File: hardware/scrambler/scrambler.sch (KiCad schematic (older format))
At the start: 20 parts, among them J1 Input, J2 Output, J3 Display

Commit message: Rev 1.1 of scrambler Software for scrambler
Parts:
- added R7: 330, Resistor_THT:R_Axial_DIN0207_L6.3mm_D2.5mm_P10.16mm_Horizontal, symbol Device:R_US
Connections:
- wire segments 82 -> 87
- no-connect marks 12 -> 10
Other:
- moved on the sheet: D1, D2, D3, D4, D5, D6, J1, R1, R2, R3, R4, R5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

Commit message: Fixup libraries. Rebrand.
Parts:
- A1: symbol MCU_Module:Arduino_UNO_R3 -> DMXDemonstrator:Arduino_UNO_R3-MCU_Module
- S1, S2, S3: symbol SparkFun-Switches:MOMENTARY-SWITCH-SPST-PTH-12MM -> DMXDemonstrator:MOMENTARY-SWITCH-SPST-PTH-12MM-SparkFun-Switches
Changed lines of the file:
@@
 EESchema Schematic File Version 4
-LIBS:scrambler-cache
-EELAYER 26 0
+EELAYER 30 0
 EELAYER END
 $Descr A4 11693 8268
@@
 Date "2023-12-24"
 Rev "1.1"
-Comp "Crazy Giraffe Software"
+Comp "Sparky Bobo Designs"
 Comment1 ""
 Comment2 "Designed by: SparkyBobo"
@@
 $EndDescr
 $Comp
-L MCU_Module:Arduino_UNO_R3 A1
+L DMXDemonstrator:Arduino_UNO_R3-MCU_Module A1
 U 1 1 5F3035A0
 P 6200 3350
@@
 Connection ~ 4250 3850
 $Comp
-L SparkFun-Switches:MOMENTARY-SWITCH-SPST-PTH-12MM S1
+L DMXDemonstrator:MOMENTARY-SWITCH-SPST-PTH-12MM-SparkFun-Switches S1
 U 1 1 5F53A7F8
 P 4550 3200
@@
 $EndComp
 $Comp
-L SparkFun-Switches:MOMENTARY-SWITCH-SPST-PTH-12MM S2
+L DMXDemonstrator:MOMENTARY-SWITCH-SPST-PTH-12MM-SparkFun-Switches S2
 U 1 1 5F53A858
 P 4550 3550
@@
 $EndComp
 $Comp
-L SparkFun-Switches:MOMENTARY-SWITCH-SPST-PTH-12MM S3
+L DMXDemonstrator:MOMENTARY-SWITCH-SPST-PTH-12MM-SparkFun-Switches S3
 U 1 1 5F53A8A0
 P 4550 3850

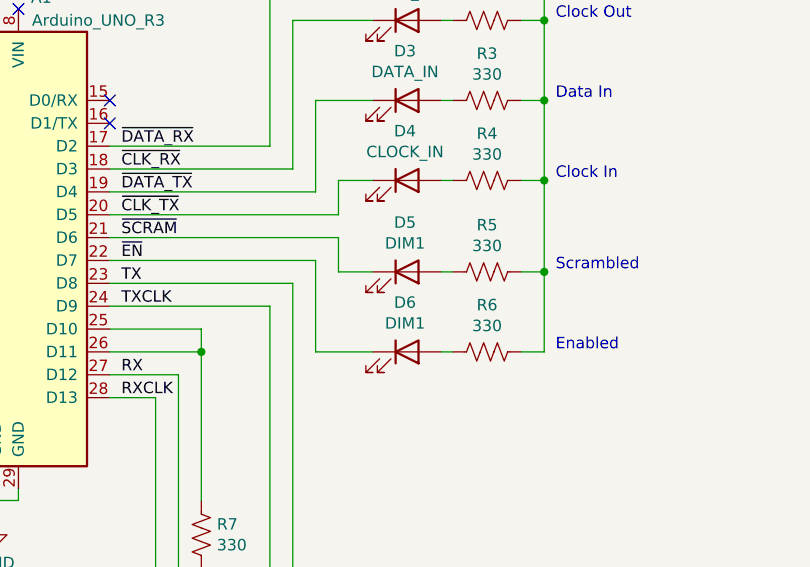
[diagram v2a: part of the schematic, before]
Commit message: Users/sparky/hwcleanup (#22)
* Rename control-pro
Update readmes
Delete old pngs

* Add PWM headers on DMX-RX1.

* Add BOM generator
Add BOM and parts .md's
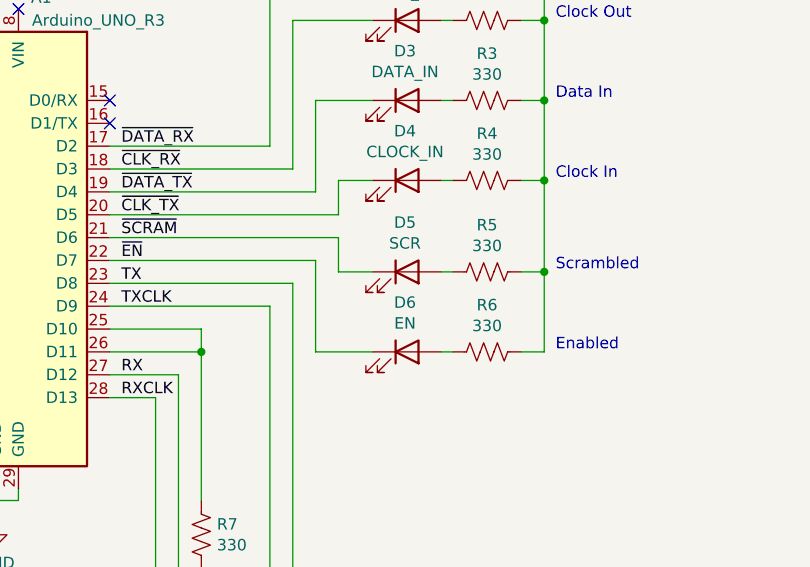
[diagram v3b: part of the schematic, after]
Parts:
- A1: PArtId2 (none) -> H_ARDUINO; PartId0 (none) -> PCB_FS1; PartId1 (none) -> A_ARDUINO
- D1, D3: PartId (none) -> LED_GRN
- D2, D4: PartId (none) -> LED_RED
- D5: value DIM1 -> SCR; PartId (none) -> LED_RED
- D6: value DIM1 -> EN; PartId (none) -> LED_GRN
- J1: PartId (none) -> H_1x3_RA,JP_1x3
- J2, J3: PartId (none) -> H_1x3_RA
- R1, R2, R3, R4, R5, R6, R7: PartId (none) -> R_LED
- S1, S2, S3: Field4 SWCH-09185 -> (none); PartId (none) -> S_MOM
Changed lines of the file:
@@
 F 2 "footprints:ARDUINO_R3_NO_HOLES" H 6350 2300 50  0001 L CNN
 F 3 "https://www.arduino.cc/en/Main/arduinoBoardUno" H 6000 4400 50  0001 C CNN
+F 4 "PCB_FS1" H 6200 3350 50  0001 C CNN "PartId0"
+F 5 "A_ARDUINO" H 6200 3350 50  0001 C CNN "PartId1"
+F 6 "H_ARDUINO" H 6200 3350 50  0001 C CNN "PArtId2"
 	1    6200 3350
 	-1   0    0    -1
@@
 F 2 "Connector_PinHeader_2.54mm:PinHeader_1x03_P2.54mm_Horizontal" H 4300 5000 50  0001 C CNN
 F 3 "~" H 4300 5000 50  0001 C CNN
+F 4 "H_1x3_RA" H 4300 5000 50  0001 C CNN "PartId"
 	1    4300 5000
 	-1   0    0    -1
@@
 F 2 "LED_THT:LED_D5.0mm" H 8000 2050 50  0001 C CNN
 F 3 "~" H 8000 2050 50  0001 C CNN
+F 4 "LED_GRN" H 8000 2050 50  0001 C CNN "PartId"
 	1    8000 2050
 	1    0    0    -1
@@
 F 2 "Resistor_THT:R_Axial_DIN0207_L6.3mm_D2.5mm_P10.16mm_Horizontal" V 8390 2040 50  0001 C CNN
 F 3 "~" H 8350 2050 50  0001 C CNN
+F 4 "R_LED" V 8350 2050 50  0001 C CNN "PartId"
 	1    8350 2050
 	0    1    1    0
@@
 F 2 "LED_THT:LED_D5.0mm" H 8000 2400 50  0001 C CNN
 F 3 "~" H 8000 2400 50  0001 C CNN
+F 4 "LED_RED" H 8000 2400 50  0001 C CNN "PartId"
 	1    8000 2400
 	1    0    0    -1
@@
 F 2 "Resistor_THT:R_Axial_DIN0207_L6.3mm_D2.5mm_P10.16mm_Horizontal" V 8390 2390 50  0001 C CNN
 F 3 "~" H 8350 2400 50  0001 C CNN
+F 4 "R_LED" V 8350 2400 50  0001 C CNN "PartId"
 	1    8350 2400
 	0    1    1    0
@@
 F 2 "LED_THT:LED_D5.0mm" H 8000 3100 50  0001 C CNN
 F 3 "~" H 8000 3100 50  0001 C CNN
+F 4 "LED_RED" H 8000 3100 50  0001 C CNN "PartId"
 	1    8000 3100
 	1    0    0    -1
@@
 F 2 "Resistor_THT:R_Axial_DIN0207_L6.3mm_D2.5mm_P10.16mm_Horizontal" V 8390 3090 50  0001 C CNN
 F 3 "~" H 8350 3100 50  0001 C CNN
+F 4 "R_LED" V 8350 3100 50  0001 C CNN "PartId"
 	1    8350 3100
 	0    1    1    0
@@
 F 2 "LED_THT:LED_D5.0mm" H 8000 2750 50  0001 C CNN
 F 3 "~" H 8000 2750 50  0001 C CNN
+F 4 "LED_GRN" H 8000 2750 50  0001 C CNN "PartId"
 	1    8000 2750
 	1    0    0    -1
@@
 F 2 "Resistor_THT:R_Axial_DIN0207_L6.3mm_D2.5mm_P10.16mm_Horizontal" V 8390 2740 50  0001 C CNN
 F 3 "~" H 8350 2750 50  0001 C CNN
+F 4 "R_LED" V 8350 2750 50  0001 C CNN "PartId"
 	1    8350 2750
 	0    1    1    0
@@
 F 2 "Switches:TACTILE_SWITCH_PTH_12MM" H 4550 3400 20  0001 C CNN
 F 3 "" H 4550 3200 50  0001 C CNN
-F 4 "SWCH-09185" H 4550 3331 60  0001 C CNN "Field4"
+F 4 "S_MOM" H 4550 3200 50  0001 C CNN "PartId"
 	1    4550 3200
 	1    0    0    -1
@@
 F 2 "Switches:TACTILE_SWITCH_PTH_12MM" H 4550 3750 20  0001 C CNN
 F 3 "" H 4550 3550 50  0001 C CNN
-F 4 "SWCH-09185" H 4550 3681 60  0001 C CNN "Field4"
+F 4 "S_MOM" H 4550 3681 60  0001 C CNN "PartId"
 	1    4550 3550
 	1    0    0    -1
@@
 F 2 "Switches:TACTILE_SWITCH_PTH_12MM" H 4550 4050 20  0001 C CNN
 F 3 "" H 4550 3850 50  0001 C CNN
-F 4 "SWCH-09185" H 4550 3981 60  0001 C CNN "Field4"
+F 4 "S_MOM" H 4550 3981 60  0001 C CNN "PartId"
 	1    4550 3850
 	1    0    0    -1
@@
 F 2 "Resistor_THT:R_Axial_DIN0207_L6.3mm_D2.5mm_P10.16mm_Horizontal" V 8390 3490 50  0001 C CNN
 F 3 "~" H 8350 3500 50  0001 C CNN
+F 4 "R_LED" V 8350 3500 50  0001 C CNN "PartId"
 	1    8350 3500
 	0    1    1    0
@@
 P 8000 3500
 F 0 "D5" H 7991 3716 50  0000 C CNN
-F 1 "DIM1" H 7991 3625 50  0000 C CNN
+F 1 "SCR" H 7991 3625 50  0000 C CNN
 F 2 "LED_THT:LED_D5.0mm" H 8000 3500 50  0001 C CNN
 F 3 "~" H 8000 3500 50  0001 C CNN
+F 4 "LED_RED" H 8000 3500 50  0001 C CNN "PartId"
 	1    8000 3500
 	1    0    0    -1
@@
 F 2 "Connector_PinHeader_2.54mm:PinHeader_1x03_P2.54mm_Horizontal" H 8550 5000 50  0001 C CNN
 F 3 "~" H 8550 5000 50  0001 C CNN
+F 4 "H_1x3_RA,JP_1x3" H 8550 5000 50  0001 C CNN "PartId"
 	1    8550 5000
 	1    0    0    -1
@@
 F 2 "Resistor_THT:R_Axial_DIN0207_L6.3mm_D2.5mm_P10.16mm_Horizontal" V 8390 3840 50  0001 C CNN
 F 3 "~" H 8350 3850 50  0001 C CNN
+F 4 "R_LED" V 8350 3850 50  0001 C CNN "PartId"
 	1    8350 3850
 	0    1    1    0
@@
 P 8000 3850
 F 0 "D6" H 7991 4066 50  0000 C CNN
-F 1 "DIM1" H 7991 3975 50  0000 C CNN
+F 1 "EN" H 7991 3975 50  0000 C CNN
 F 2 "LED_THT:LED_D5.0mm" H 8000 3850 50  0001 C CNN
 F 3 "~" H 8000 3850 50  0001 C CNN
+F 4 "LED_GRN" H 8000 3850 50  0001 C CNN "PartId"
 	1    8000 3850
 	1    0    0    -1
@@
 F 2 "Connector_PinHeader_2.54mm:PinHeader_1x03_P2.54mm_Horizontal" H 4300 4500 50  0001 C CNN
 F 3 "~" H 4300 4500 50  0001 C CNN
+F 4 "H_1x3_RA" H 4300 4500 50  0001 C CNN "PartId"
 	1    4300 4500
 	-1   0    0    -1
@@
 F 2 "Resistor_THT:R_Axial_DIN0207_L6.3mm_D2.5mm_P10.16mm_Horizontal" V 7140 4640 50  0001 C CNN
 F 3 "~" H 7100 4650 50  0001 C CNN
+F 4 "R_LED" H 7100 4650 50  0001 C CNN "PartId"
 	1    7100 4650
 	1    0    0    -1
